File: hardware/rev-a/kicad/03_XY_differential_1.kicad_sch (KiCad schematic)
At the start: 16 parts, among them U5 NJM4580DD, U6 NJM4580DD

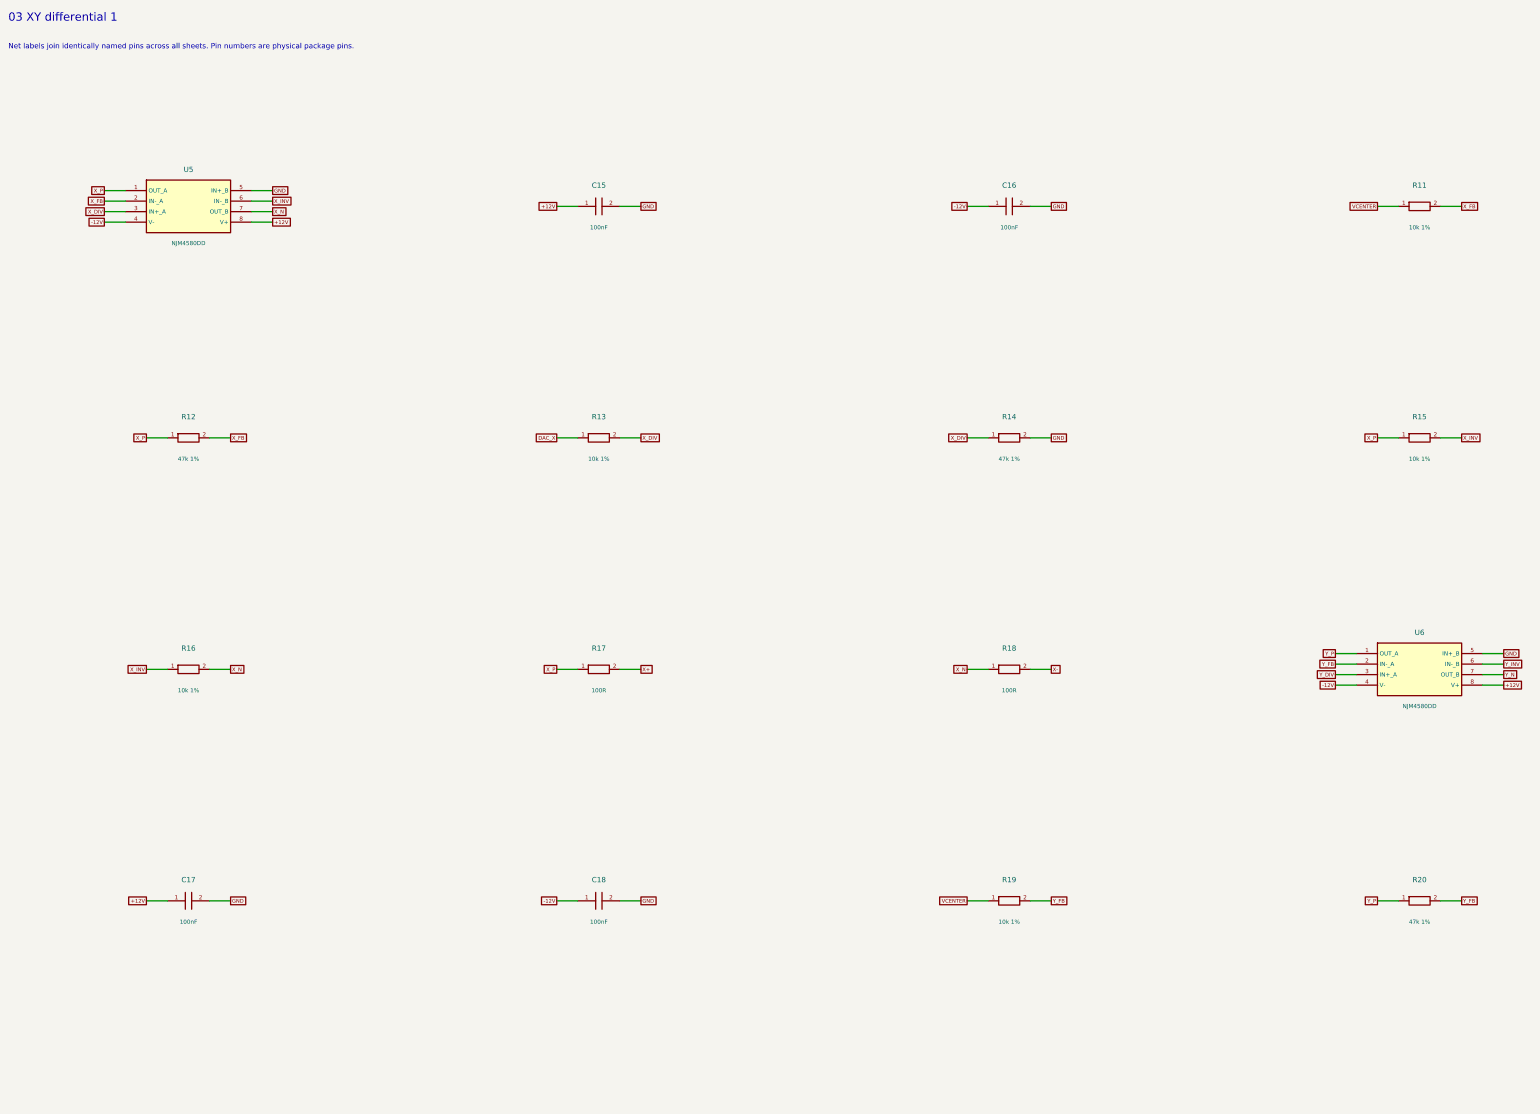
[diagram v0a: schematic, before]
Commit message: Redraw Rev.A schematics with functional blocks and explicit wiring
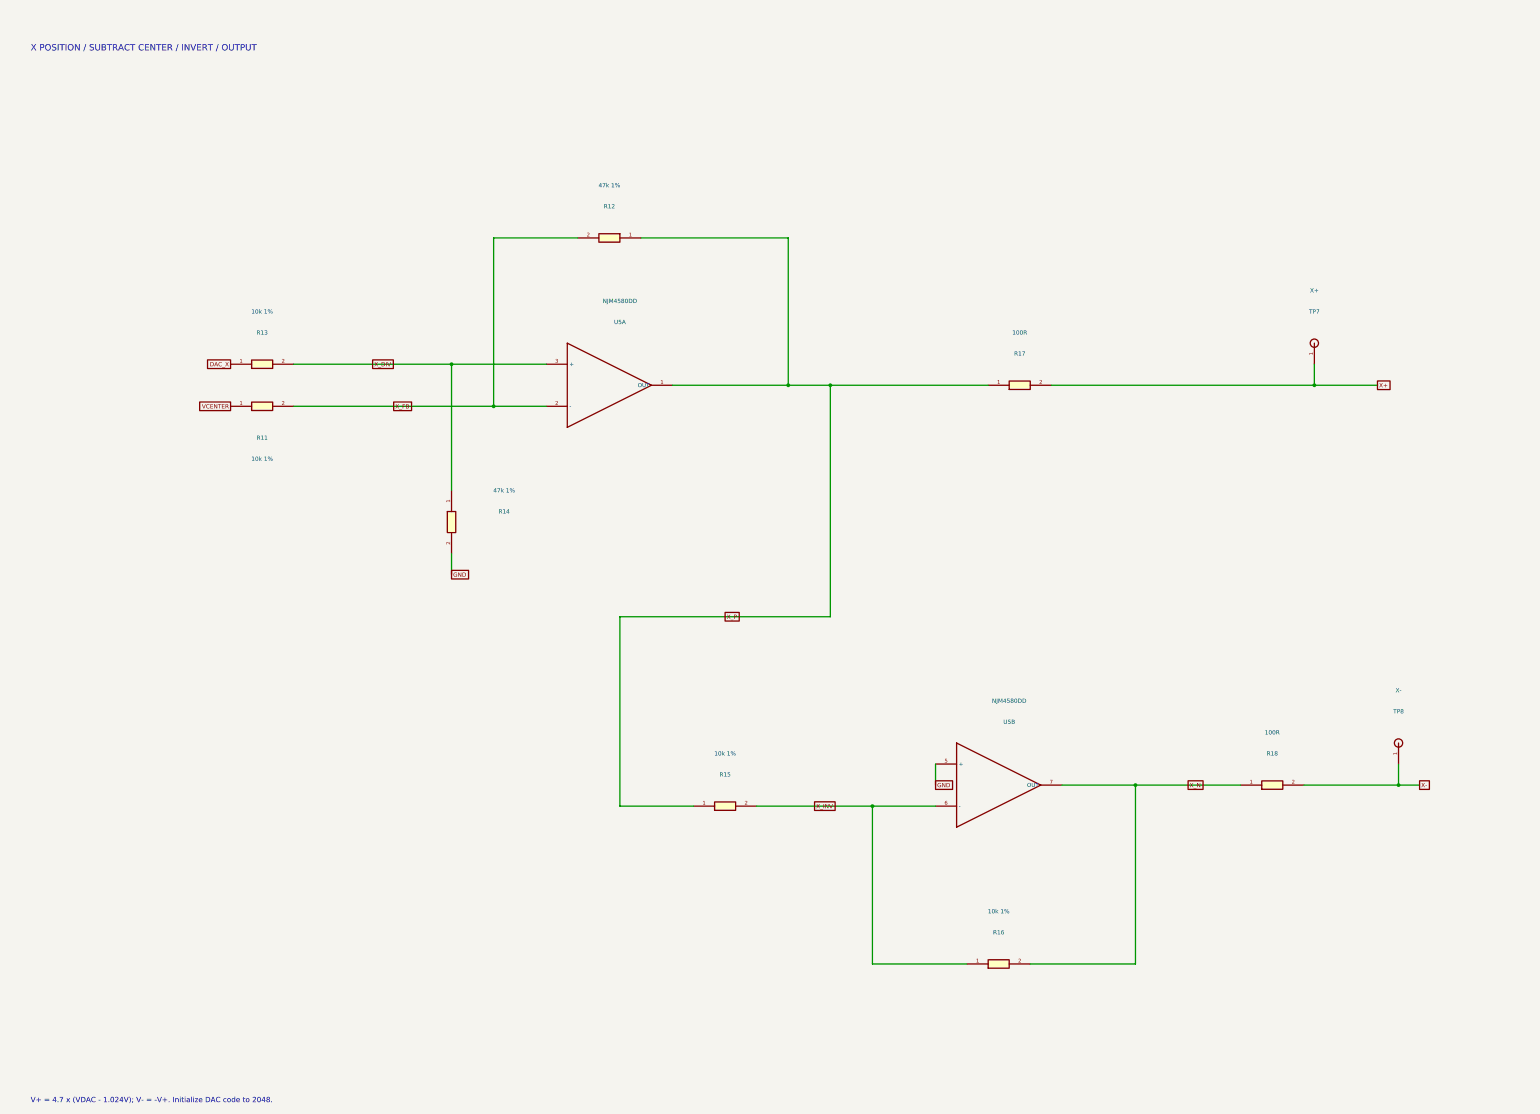
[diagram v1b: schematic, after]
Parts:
- removed C15, C16, C17, C18: 100nF, RevA:C_Disc_D5.0mm_W2.5mm_P5.00mm, symbol RevA:C
- removed R19: 10k 1%, RevA:R_Axial_DIN0207_L6.3mm_D2.5mm_P10.16mm_Horizontal, symbol RevA:R
- removed R20: 47k 1%, RevA:R_Axial_DIN0207_L6.3mm_D2.5mm_P10.16mm_Horizontal, symbol RevA:R
- removed U6: NJM4580DD, RevA:DIP-8_W7.62mm, symbol RevA:Opamp
- added TP7: X+, RevA:TestPoint_THTPad_D2.0mm_Drill1.0mm, symbol RevA:TP
- added TP8: X-, RevA:TestPoint_THTPad_D2.0mm_Drill1.0mm, symbol RevA:TP
- added unit 2 of U5
- U5: symbol RevA:Opamp -> RevA:AMP
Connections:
- net GND: now also U5.5 (+); no longer U5.5 (IN+_B)
- net X+: now also TP7.1
- net X-: now also TP8.1
- net X_INV: now also U5.6 (-); no longer U5.6 (IN-_B)
- net X_N: now also U5.7 (OUT); no longer U5.7 (OUT_B)
- removed net +12V: U5.8 (V+)
- removed net -12V: U5.4 (V-)
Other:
- note added: "V+ = 4.7 x (VDAC - 1.024V); V- = -V+. Initialize DAC code to 2048."
- note added: "X POSITION / SUBTRACT CENTER / INVERT / OUTPUT"
- note removed: "03 XY differential 1"
- note removed: "Net labels join identically named pins across all sheets. Pin numbers are physical package pins."
- company: CoreS3 ILDA evaluation -> (none)
- title: 03_XY_differential_1 -> X / Differential position driver
